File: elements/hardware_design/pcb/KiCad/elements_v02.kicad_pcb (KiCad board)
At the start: 2 copper layers, 164.5 x 106 mm, 198 parts, among them IC1 LM4040B10, IC10 STM32F405RGT6, IC11 4051PW, IC12 WM8731, IC13 MCP6004, IC14 LME49720, IC2 LM1117-3.3, IC3 4051PW, IC4 LM1117-3.3, IC5 4051PW, IC6 MCP6004, IC7 MCP6004, IC8 4051PW, IC9 MCP6002, J1 PJ301_THONKICONN6, J10 PJ301_THONKICONN6, J11 PJ301_THONKICONN6, J12 PJ301_THONKICONN6, J13 PJ301_THONKICONN6, J14 PJ301_THONKICONN6, J15 PJ301_THONKICONN6, J16 PJ301_THONKICONN6, J17 PJ301_THONKICONN6, J18 PJ301_THONKICONN6, J2 PJ301_THONKICONN6, J3 PJ301_THONKICONN6, J4 PJ301_THONKICONN6, J5 PJ301_THONKICONN6, J6 PJ301_THONKICONN6, J7 PJ301_THONKICONN6, J8 PJ301_THONKICONN6, J9 PJ301_THONKICONN6, Q1 8MHz, Q2 MMBT3904, SW1 LP4OA1PBCT

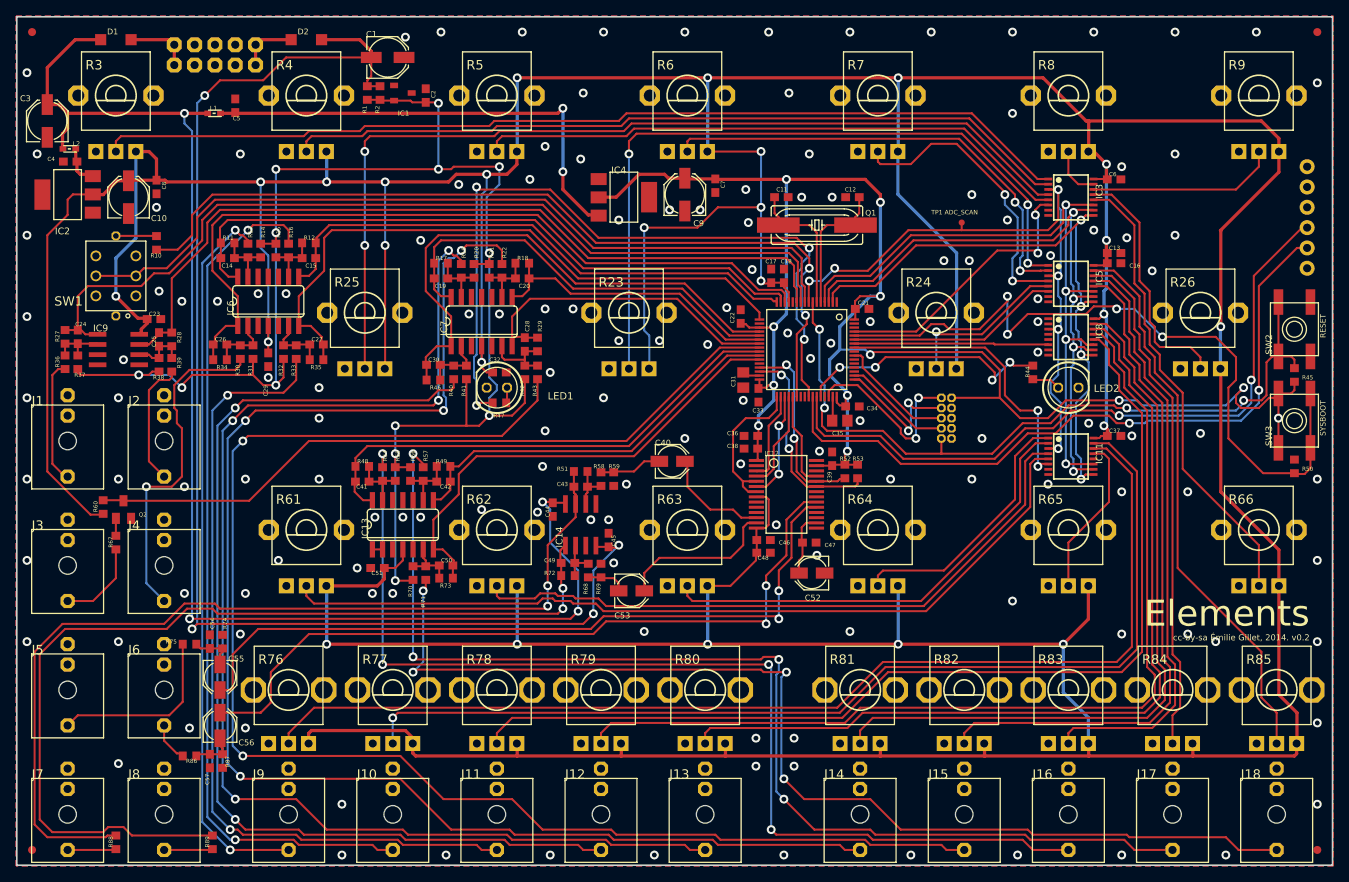
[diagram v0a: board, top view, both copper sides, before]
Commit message: Marbles added
Beware! T_clock is shorted to ground. Fix before using this PCB
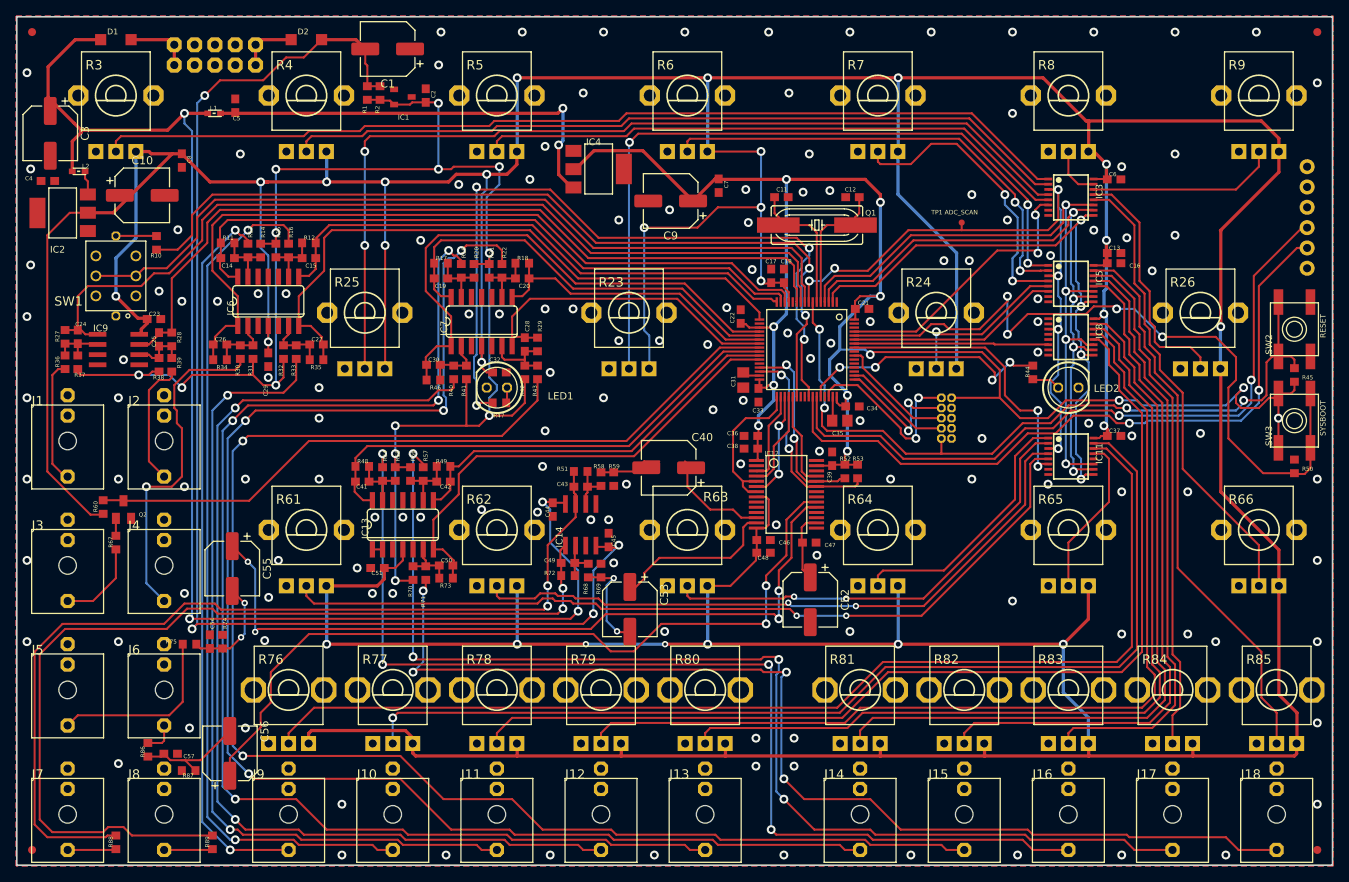
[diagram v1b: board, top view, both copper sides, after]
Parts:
- removed U$2: , elements_v02:ROHS_BIG
- C1, C10, C3, C9: footprint elements_v02:PANASONIC_C -> Capacitor_SMD:CP_Elec_6.3x5.9
- C40, C52, C53, C55, C56: footprint elements_v02:PANASONIC_B -> Capacitor_SMD:CP_Elec_6.3x5.4
- JP2: value (none) -> M06SIP
- L1, L2: value (none) -> WE-CBF_0603
- SW2, SW3: value (none) -> EVQQ2
- moved C55 13.7 mm to (93.2, 121.0)
- moved R86 5.27 mm to (82.7, 143.6), turned to 90 degrees
- moved C57 4.98 mm to (85.5, 144.1), turned to 0 degrees
- moved IC4 4.73 mm to (139.0, 71.0)
- moved C8 4.58 mm to (86.9, 70.0)
- moved R87 4.40 mm to (87.8, 146.2), turned to 0 degrees
- moved C56 3.70 mm to (92.9, 144.1)
- moved C4 3.69 mm to (70.2, 72.5)
- moved C52 3.34 mm to (165.4, 124.8), turned to -90 degrees
- moved L2 3.04 mm to (74.1, 71.3)
- moved IC2 2.38 mm to (72.0, 76.5)
- moved C53 2.32 mm to (142.9, 126.0), turned to -90 degrees
- moved C9 1.94 mm to (148.0, 75.0), turned to 180 degrees
- moved C10 1.73 mm to (82.0, 74.3), turned to 0 degrees
- moved C3 1.60 mm to (70.5, 66.5), turned to -90 degrees
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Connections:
- C11 pad 2: N$8 -> (no net)
- C12 pad 2: N$7 -> (no net)
- C14 pad 1: N$5 -> (no net)
- C15 pad 1: N$2 -> (no net)
- C19 pad 1: N$9 -> (no net)
- C20 pad 1: N$14 -> (no net)
- C24 pad 1: N$11 -> (no net)
- C25 pad 1: N$15 -> (no net)
- C26 pad 1: N$42 -> (no net)
- C27 pad 1: N$27 -> (no net)
- C28 pad 1: N$37 -> (no net)
- C30 pad 1: N$24 -> (no net)
- C31 pad 1: N$19 -> (no net)
- C35 pad 1: N$13 -> (no net)
- C4 pad 1: N$80 -> (no net)
- C41 pad 1: N$40 -> (no net)
- C42 pad 1: N$30 -> (no net)
- C43 pad 1: N$25 -> (no net)
- C43 pad 2: N$28 -> (no net)
- C47 pad 1: N$17 -> Net-(IC12-VMID)
- C49 pad 1: N$32 -> (no net)
- C49 pad 2: N$33 -> (no net)
- C5 pad 1: N$61 -> (no net)
- C50 pad 1: N$35 -> (no net)
- C54 pad 1: N$22 -> Net-(C54-Pad1)
- C57 pad 1: N$18 -> Net-(C56-Pad-)
- D1 pad A: N$56 -> (no net)
- D2 pad C: N$64 -> (no net)
- IC10 pad 29: I2C_SCL -> (no net)
- IC10 pad 30: I2C_SDA -> (no net)
- IC10 pad 31: N$19 -> Net-(IC10-VCAP_1)
- IC10 pad 33: I2S_LRCK -> (no net)
- IC10 pad 34: I2S_SCK -> (no net)
- IC10 pad 35: I2S_SIN -> (no net)
- IC10 pad 36: I2S_SOUT -> (no net)
- IC10 pad 37: I2S_MCK -> (no net)
- IC10 pad 41: N$79 -> (no net)
- IC10 pad 42: TX -> (no net)
- IC10 pad 43: RX -> (no net)
- IC10 pad 44: N$54 -> (no net)
- IC10 pad 46: JTMS -> (no net)
- IC10 pad 47: N$13 -> Net-(IC10-VCAP_2)
- IC10 pad 49: JTCK -> (no net)
- IC10 pad 5: N$7 -> Net-(IC10-PD0/OSC_IN)
- IC10 pad 50: JTDI -> (no net)
- IC10 pad 55: JTDO -> (no net)
- IC10 pad 6: N$8 -> Net-(IC10-PD1/OSC_OUT)
- IC10 pad 60: BOOT_FLASH -> (no net)
- IC10 pad 7: RESET -> (no net)
- IC11 pad 1: N$48 -> (no net)
- IC11 pad 13: N$46 -> (no net)
- IC11 pad 14: N$45 -> (no net)
- IC11 pad 15: N$47 -> (no net)
- IC11 pad 2: N$52 -> (no net)
- IC11 pad 4: N$53 -> (no net)
- IC11 pad 5: N$49 -> (no net)
- IC12 pad 16: N$17 -> Net-(IC12-VMID)
- IC12 pad 23: I2C_SDA -> /elements_v02_1/I2C_SDA
- IC12 pad 24: I2C_SCL -> /elements_v02_1/I2C_SCL
- IC12 pad 25: I2S_MCK -> /elements_v02_1/I2S_MCK
- IC12 pad 3: I2S_SCK -> /elements_v02_1/I2S_SCK
- IC12 pad 4: I2S_SOUT -> /elements_v02_1/I2S_SOUT
- IC12 pad 5: I2S_LRCK -> /elements_v02_1/I2S_LRCK
- IC12 pad 6: I2S_SIN -> /elements_v02_1/I2S_SIN
- IC12 pad 7: I2S_LRCK -> /elements_v02_1/I2S_LRCK
- IC13 pad 1: N$44 -> (no net)
- IC13 pad 13: N$40 -> Net-(IC13D--IN)
- IC13 pad 2: N$44 -> (no net)
- IC13 pad 6: N$35 -> Net-(IC13B--IN)
- IC13 pad 9: N$30 -> Net-(IC13C--IN)
- IC14 pad 1: N$33 -> Net-(IC14A-OUT)
- IC14 pad 2: N$32 -> Net-(IC14A--IN)
- IC14 pad 6: N$25 -> Net-(IC14B--IN)
- IC14 pad 7: N$28 -> Net-(IC14B-OUT)
- IC2 pad 3: N$80 -> Net-(IC2-VIN)
- IC3 pad 1: N$74 -> (no net)
- IC3 pad 12: N$55 -> (no net)
- IC3 pad 13: N$62 -> (no net)
- IC3 pad 14: N$68 -> (no net)
- IC3 pad 15: N$63 -> (no net)
- IC3 pad 2: N$73 -> (no net)
- IC3 pad 4: N$72 -> (no net)
- IC3 pad 5: N$75 -> (no net)
- IC4 pad 3: N$61 -> Net-(IC4-VIN)
- IC5 pad 1: N$71 -> (no net)
- IC5 pad 12: N$65 -> (no net)
- IC5 pad 13: N$76 -> (no net)
- IC5 pad 14: N$77 -> (no net)
- IC5 pad 15: N$78 -> (no net)
- IC5 pad 2: N$69 -> (no net)
- IC5 pad 4: N$67 -> (no net)
- IC5 pad 5: N$70 -> (no net)
- IC6 pad 13: N$5 -> Net-(IC6D--IN)
- IC6 pad 2: N$42 -> Net-(IC6A--IN)
- IC6 pad 6: N$27 -> Net-(IC6B--IN)
- IC6 pad 9: N$2 -> Net-(IC6C--IN)
- IC7 pad 13: N$9 -> Net-(IC7D--IN)
- IC7 pad 2: N$24 -> Net-(IC7A--IN)
- IC7 pad 6: N$37 -> Net-(IC7B--IN)
- IC7 pad 9: N$14 -> Net-(IC7C--IN)
- IC8 pad 12: N$51 -> (no net)
- IC8 pad 13: N$58 -> (no net)
- IC8 pad 14: N$50 -> (no net)
- IC8 pad 15: N$57 -> (no net)
- IC9 pad 2: N$11 -> Net-(IC9A--IN)
- IC9 pad 6: N$15 -> Net-(IC9B--IN)
- J1 pad P3: N$10 -> (no net)
- J10 pad P3: N$1 -> (no net)
- J11 pad P3: N$26 -> (no net)
- J12 pad P3: N$16 -> (no net)
- J13 pad P3: N$3 -> (no net)
- J14 pad P3: N$12 -> (no net)
- J15 pad P3: N$36 -> (no net)
- J16 pad P3: N$39 -> (no net)
- J17 pad P3: N$29 -> (no net)
- J18 pad P3: N$34 -> (no net)
- J2 pad P3: N$6 -> (no net)
- J3 pad P3: N$43 -> (no net)
- J4 pad P3: N$41 -> (no net)
- J5 pad P3: N$20 -> (no net)
- J6 pad P3: N$21 -> (no net)
- J7 pad P3: ROUT_JACK -> (no net)
- J8 pad P3: LOUT_JACK -> (no net)
- J9 pad P3: N$4 -> (no net)
- JP1 pad 10: RESET -> /elements_v02_1/RESET
- JP1 pad 2: JTMS -> /elements_v02_1/JTMS
- JP1 pad 4: JTCK -> /elements_v02_1/JTCK
- JP1 pad 6: JTDO -> /elements_v02_1/JTDO
- JP1 pad 8: JTDI -> /elements_v02_1/JTDI
- JP2 pad 4: RX -> /elements_v02_1/RX
- JP2 pad 5: TX -> /elements_v02_1/TX
- JP3 pad 1: N$56 -> Net-(D1-PadA)
- JP3 pad 10: N$64 -> Net-(D2-PadC)
- JP3 pad 2: N$56 -> Net-(D1-PadA)
- JP3 pad 9: N$64 -> Net-(D2-PadC)
- L1 pad 2: N$61 -> Net-(IC4-VIN)
- L2 pad 2: N$80 -> Net-(IC2-VIN)
- LED1 pad A: N$60 -> (no net)
- LED2 pad A: N$59 -> (no net)
- Q1 pad 1: N$8 -> Net-(IC10-PD1/OSC_OUT)
- Q1 pad 2: N$7 -> Net-(IC10-PD0/OSC_IN)
- Q2 pad B: N$66 -> (no net)
- R10 pad 2: N$38 -> (no net)
- R11 pad 2: N$5 -> Net-(IC6D--IN)
- R12 pad 2: N$2 -> Net-(IC6C--IN)
- R13 pad 1: N$5 -> Net-(IC6D--IN)
- R13 pad 2: N$4 -> Net-(J9-3)
- R14 pad 1: N$5 -> Net-(IC6D--IN)
- R15 pad 1: N$2 -> Net-(IC6C--IN)
- R16 pad 1: N$2 -> Net-(IC6C--IN)
- R16 pad 2: N$1 -> Net-(J10-3)
- R17 pad 2: N$9 -> Net-(IC7D--IN)
- R18 pad 2: N$14 -> Net-(IC7C--IN)
- R19 pad 1: N$9 -> Net-(IC7D--IN)
- R19 pad 2: N$3 -> Net-(J13-3)
- R20 pad 1: N$9 -> Net-(IC7D--IN)
- R21 pad 1: N$14 -> Net-(IC7C--IN)
- R22 pad 1: N$14 -> Net-(IC7C--IN)
- R22 pad 2: N$12 -> Net-(J14-3)
- R23 pad P$2: N$71 -> Net-(IC5A-X4)
- R24 pad P$2: N$70 -> Net-(IC5A-X5)
- R25 pad P$2: N$72 -> Net-(IC3A-X7)
- R26 pad P$2: N$62 -> Net-(IC3A-X0)
- R27 pad 2: N$11 -> Net-(IC9A--IN)
- R28 pad 2: N$15 -> Net-(IC9B--IN)
- R29 pad 2: N$37 -> Net-(IC7B--IN)
- R3 pad P$2: N$74 -> Net-(IC3A-X4)
- R30 pad 1: N$42 -> Net-(IC6A--IN)
- R30 pad 2: N$41 -> Net-(J4-3)
- R31 pad 1: N$42 -> Net-(IC6A--IN)
- R32 pad 1: N$27 -> Net-(IC6B--IN)
- R33 pad 1: N$27 -> Net-(IC6B--IN)
- R33 pad 2: N$26 -> Net-(J11-3)
- R34 pad 2: N$42 -> Net-(IC6A--IN)
- R35 pad 2: N$27 -> Net-(IC6B--IN)
- R36 pad 1: N$11 -> Net-(IC9A--IN)
- R36 pad 2: N$10 -> Net-(J1-3)
- R37 pad 1: N$11 -> Net-(IC9A--IN)
- R38 pad 1: N$15 -> Net-(IC9B--IN)
- R39 pad 1: N$15 -> Net-(IC9B--IN)
- R39 pad 2: N$6 -> Net-(J2-3)
- R4 pad P$2: N$73 -> Net-(IC3A-X6)
- R40 pad 1: N$24 -> Net-(IC7A--IN)
- R40 pad 2: N$16 -> Net-(J12-3)
- R41 pad 1: N$24 -> Net-(IC7A--IN)
- R42 pad 1: N$37 -> Net-(IC7B--IN)
- R43 pad 1: N$37 -> Net-(IC7B--IN)
- R43 pad 2: N$36 -> Net-(J15-3)
- R44 pad 1: N$54 -> Net-(IC10-PA11/USART1_CTS/CANRX/USBDM/TIM1_CH4)
- R44 pad 2: N$59 -> Net-(LED2-PadA)
- R45 pad 1: RESET -> /elements_v02_1/RESET
- R46 pad 2: N$24 -> Net-(IC7A--IN)
- R47 pad 1: N$79 -> Net-(IC10-PA8/USART1_CK/TIM1_CH1/MCO)
- R47 pad 2: N$60 -> Net-(LED1-PadA)
- R48 pad 2: N$40 -> Net-(IC13D--IN)
- R49 pad 2: N$30 -> Net-(IC13C--IN)
- R5 pad P$2: N$75 -> Net-(IC3A-X5)
- R50 pad 2: BOOT_FLASH -> /elements_v02_1/BOOT_FLASH
- R51 pad 1: N$28 -> Net-(IC14B-OUT)
- R51 pad 2: N$25 -> Net-(IC14B--IN)
- R52 pad 1: I2C_SCL -> /elements_v02_1/I2C_SCL
- R53 pad 1: I2C_SDA -> /elements_v02_1/I2C_SDA
- R54 pad 1: N$40 -> Net-(IC13D--IN)
- R54 pad 2: N$39 -> Net-(J16-3)
- R55 pad 1: N$40 -> Net-(IC13D--IN)
- R56 pad 1: N$30 -> Net-(IC13C--IN)
- R57 pad 1: N$30 -> Net-(IC13C--IN)
- R57 pad 2: N$29 -> Net-(J17-3)
- R58 pad 1: N$25 -> Net-(IC14B--IN)
- R58 pad 2: N$23 -> (no net)
- R59 pad 2: N$23 -> Net-(C40-Pad-)
- R6 pad P$2: N$69 -> Net-(IC5A-X6)
- R61 pad P$2: N$49 -> Net-(IC11A-X5)
- R62 pad P$2: N$53 -> Net-(IC11A-X7)
- R63 pad P$2: N$52 -> Net-(IC11A-X6)
- R64 pad P$2: N$48 -> Net-(IC11A-X4)
- R65 pad P$2: N$46 -> Net-(IC11A-X0)
- R66 pad P$2: N$55 -> Net-(IC3A-X3)
- R67 pad 1: N$43 -> Net-(J3-3)
- R67 pad 2: N$66 -> Net-(Q2-PadB)
- R68 pad 1: N$32 -> Net-(IC14A--IN)
- R68 pad 2: N$31 -> (no net)
- R69 pad 2: N$31 -> Net-(C53-Pad-)
- R7 pad P$2: N$67 -> Net-(IC5A-X7)
- R70 pad 1: N$35 -> Net-(IC13B--IN)
- R71 pad 1: N$35 -> Net-(IC13B--IN)
- R71 pad 2: N$34 -> Net-(J18-3)
- R72 pad 1: N$33 -> Net-(IC14A-OUT)
- R72 pad 2: N$32 -> Net-(IC14A--IN)
- R73 pad 2: N$35 -> Net-(IC13B--IN)
- R74 pad 2: N$22 -> Net-(C54-Pad1)
- R75 pad 1: N$22 -> Net-(C54-Pad1)
- R75 pad 2: N$20 -> Net-(J5-3)
- R76 pad P$2: N$45 -> Net-(IC11A-X1)
- R77 pad P$2: N$47 -> Net-(IC11A-X2)
- R78 pad P$2: N$51 -> Net-(IC8A-X3)
- R79 pad P$2: N$58 -> Net-(IC8A-X0)
- R8 pad P$2: N$63 -> Net-(IC3A-X2)
- R80 pad P$2: N$50 -> Net-(IC8A-X1)
- R81 pad P$2: N$57 -> Net-(IC8A-X2)
- R82 pad P$2: N$65 -> Net-(IC5A-X3)
- R83 pad P$2: N$76 -> Net-(IC5A-X0)
- R84 pad P$2: N$77 -> Net-(IC5A-X1)
- R85 pad P$2: N$78 -> Net-(IC5A-X2)
- R86 pad 1: N$18 -> Net-(C56-Pad-)
- R86 pad 2: N$21 -> Net-(J6-3)
- R87 pad 2: N$18 -> Net-(C56-Pad-)
- R88 pad 1: ROUT_JACK -> Net-(J7-3)
- R88 pad 2: N$28 -> Net-(IC14B-OUT)
- R89 pad 1: LOUT_JACK -> Net-(J8-3)
- R89 pad 2: N$33 -> Net-(IC14A-OUT)
- R9 pad P$2: N$68 -> Net-(IC3A-X1)
- SW1 pad L1: N$38 -> Net-(R10-Pad2)
- SW2 pad B: RESET -> /elements_v02_1/RESET
- SW2 pad B': RESET -> /elements_v02_1/RESET
- SW3 pad A: BOOT_FLASH -> /elements_v02_1/BOOT_FLASH
- SW3 pad A': BOOT_FLASH -> /elements_v02_1/BOOT_FLASH
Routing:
- net N$12: track 181.5 -> 0.00 mm, vias 4 -> 0
- net Net-(J14-3): track 0.00 -> 180.7 mm, vias 0 -> 4
- net Net-(J15-3): track 0.00 -> 177.0 mm, vias 0 -> 2
- net N$36: track 177.0 -> 0.00 mm, vias 2 -> 0
- net Net-(J13-3): track 0.00 -> 158.4 mm, vias 0 -> 4
- net N$3: track 158.4 -> 0.00 mm, vias 4 -> 0
- net Net-(J17-3): track 0.00 -> 142.9 mm, vias 0 -> 4
- net N$29: track 142.9 -> 0.00 mm, vias 4 -> 0
- net Net-(IC11A-X1): track 0.00 -> 138.9 mm
- net N$45: track 138.9 -> 0.00 mm
- net Net-(J18-3): track 0.00 -> 138.1 mm, vias 0 -> 4
- net N$34: track 138.1 -> 0.00 mm, vias 4 -> 0
- net Net-(J16-3): track 0.00 -> 135.3 mm, vias 0 -> 4
- net N$39: track 135.3 -> 0.00 mm, vias 4 -> 0
- net Net-(J12-3): track 0.00 -> 130.0 mm, vias 0 -> 2
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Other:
- board text added: "Matter"
- board text added: "cc-by-sa Émilie Gillet modified by Clandestine Circutry 2024"
- board text removed: "Elements"
- board text removed: "cc-by-sa Émilie Gillet, 2014. v0.2"
